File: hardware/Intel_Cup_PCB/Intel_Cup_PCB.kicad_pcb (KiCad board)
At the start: 2 copper layers, 75 x 110 mm, 30 parts

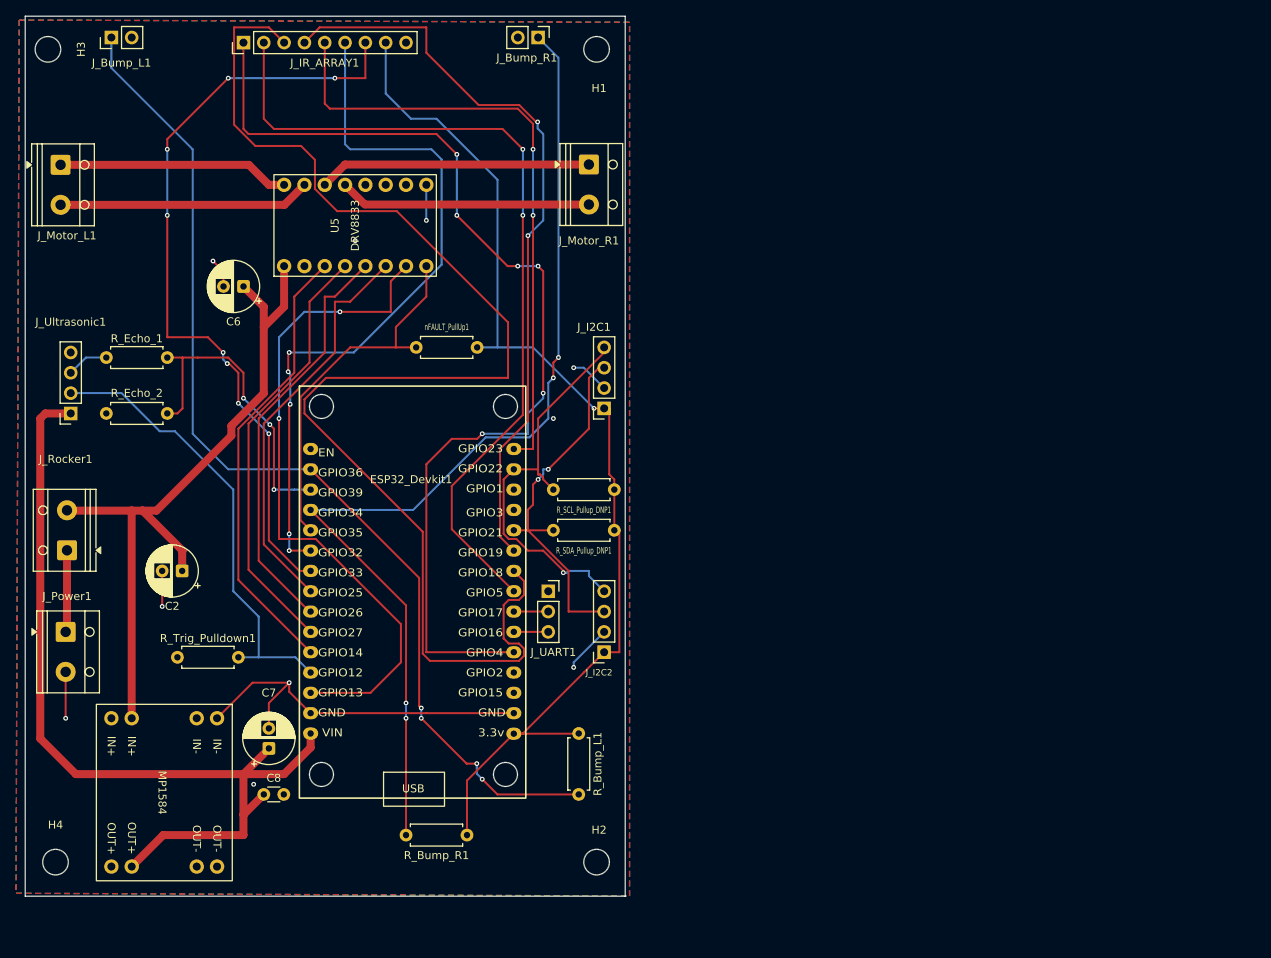
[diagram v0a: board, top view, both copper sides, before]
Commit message: Completed PCB with better ESP32 placement
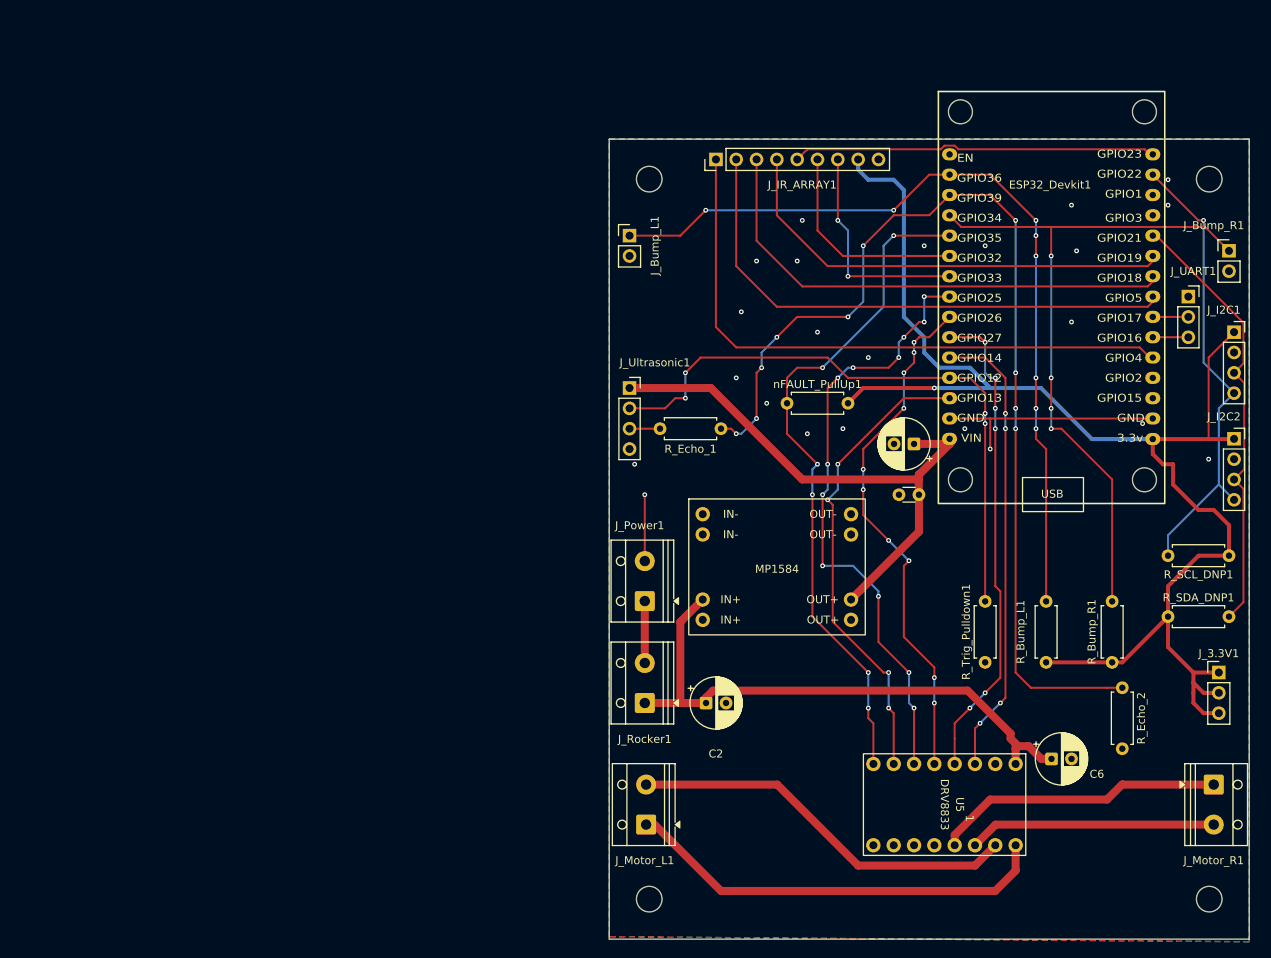
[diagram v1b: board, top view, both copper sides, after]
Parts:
- removed R_SCL_Pullup_DNP1, R_SDA_Pullup_DNP1: 4.7k, Resistor_THT:R_Axial_DIN0207_L6.3mm_D2.5mm_P7.62mm_Horizontal
- added J_3.3V1: Conn_01x03_Pin, Connector_PinHeader_2.54mm:PinHeader_1x03_P2.54mm_Vertical, F.Cu at (266.7, 129.5)
- added R_SCL_DNP1: 4.7k, Resistor_THT:R_Axial_DIN0207_L6.3mm_D2.5mm_P7.62mm_Horizontal, F.Cu at (268.0, 114.9)
- added R_SDA_DNP1: 4.7k, Resistor_THT:R_Axial_DIN0207_L6.3mm_D2.5mm_P7.62mm_Horizontal, F.Cu at (260.4, 122.6)
- moved H4 144.3 mm to (265.5, 157.9), turned to 0 degrees
- moved H3 130.1 mm to (195.5, 157.9), turned to 0 degrees
- moved R_Echo_2 124.2 mm to (254.6, 131.4), turned to -90 degrees
- moved C6 117.0 mm to (245.8, 140.3), turned to 0 degrees
- moved H2 114.7 mm to (265.5, 67.9), turned to 0 degrees
- moved U5 111.3 mm to (242.6, 139.7), turned to -90 degrees
- moved J_Motor_L1 110.3 mm to (195.1, 148.6), turned to 90 degrees
- moved J_Motor_R1 110.0 mm to (266.1, 143.6)
- moved R_Trig_Pulldown1 101.0 mm to (237.5, 128.3), turned to 90 degrees
- moved J_Bump_R1 90.4 mm to (268.0, 76.8), turned to 0 degrees
- moved C8 90.1 mm to (229.2, 107.3), turned to 180 degrees
- moved C7 89.2 mm to (228.6, 101.0), turned to 180 degrees
- moved J_I2C1 88.3 mm to (268.6, 87.0), turned to 0 degrees
- moved J_UART1 88.1 mm to (262.9, 82.5)
- moved ESP32_Devkit1 88.0 mm to (245.0, 83.3)
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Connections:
- J_Motor_R1 pad 1: /M_R_+ -> /M_R_-
- J_Motor_R1 pad 2: /M_R_- -> /M_R_+
- J_Rocker1 pad 1: Net-(J_Power1-Pin_1) -> VBAT_MOT
- J_Rocker1 pad 2: VBAT_MOT -> Net-(J_Power1-Pin_1)
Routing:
- net /IO18: track 165.2 -> 62.5 mm
- net /IO39: track 39.6 -> 130.0 mm, vias 3 -> 10
- net /IO33: track 97.8 -> 27.8 mm, vias 8 -> 2
- net /IO32: track 90.0 -> 26.7 mm, vias 5 -> 0
- net /IO4: track 129.9 -> 77.5 mm, vias 6 -> 0
- net +5V_ESP: track 113.3 -> 69.7 mm
- net /IO34: track 129.2 -> 86.8 mm
- net +3.3V: track 138.3 -> 180.5 mm
- net GND: track 77.2 -> 37.5 mm, vias 10 -> 23
- net /IO35: track 46.0 -> 85.4 mm, vias 0 -> 6
- net /IO5: track 105.6 -> 68.0 mm, vias 2 -> 0
- net /IO19: track 93.7 -> 57.1 mm, vias 2 -> 0
- net /IO23: track 77.7 -> 46.0 mm, vias 2 -> 0
- net /IO36: track 132.0 -> 104.5 mm, vias 4 -> 8
- net /IO25: track 50.5 -> 77.2 mm, vias 0 -> 12
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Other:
- board size 75 x 110 mm -> 80 x 100 mm
- board text removed: "R_Echo_2"
